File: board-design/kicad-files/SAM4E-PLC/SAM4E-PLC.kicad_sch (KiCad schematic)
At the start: 28 parts, among them J1 Conn_ARM_JTAG_SWD_10, U1 MCP7940N-xSN, U2 ATSAM4E16E, Y1 ECS-160-8-33B-CTN-TR, Y2 FC-135 32.7680KA-AG0

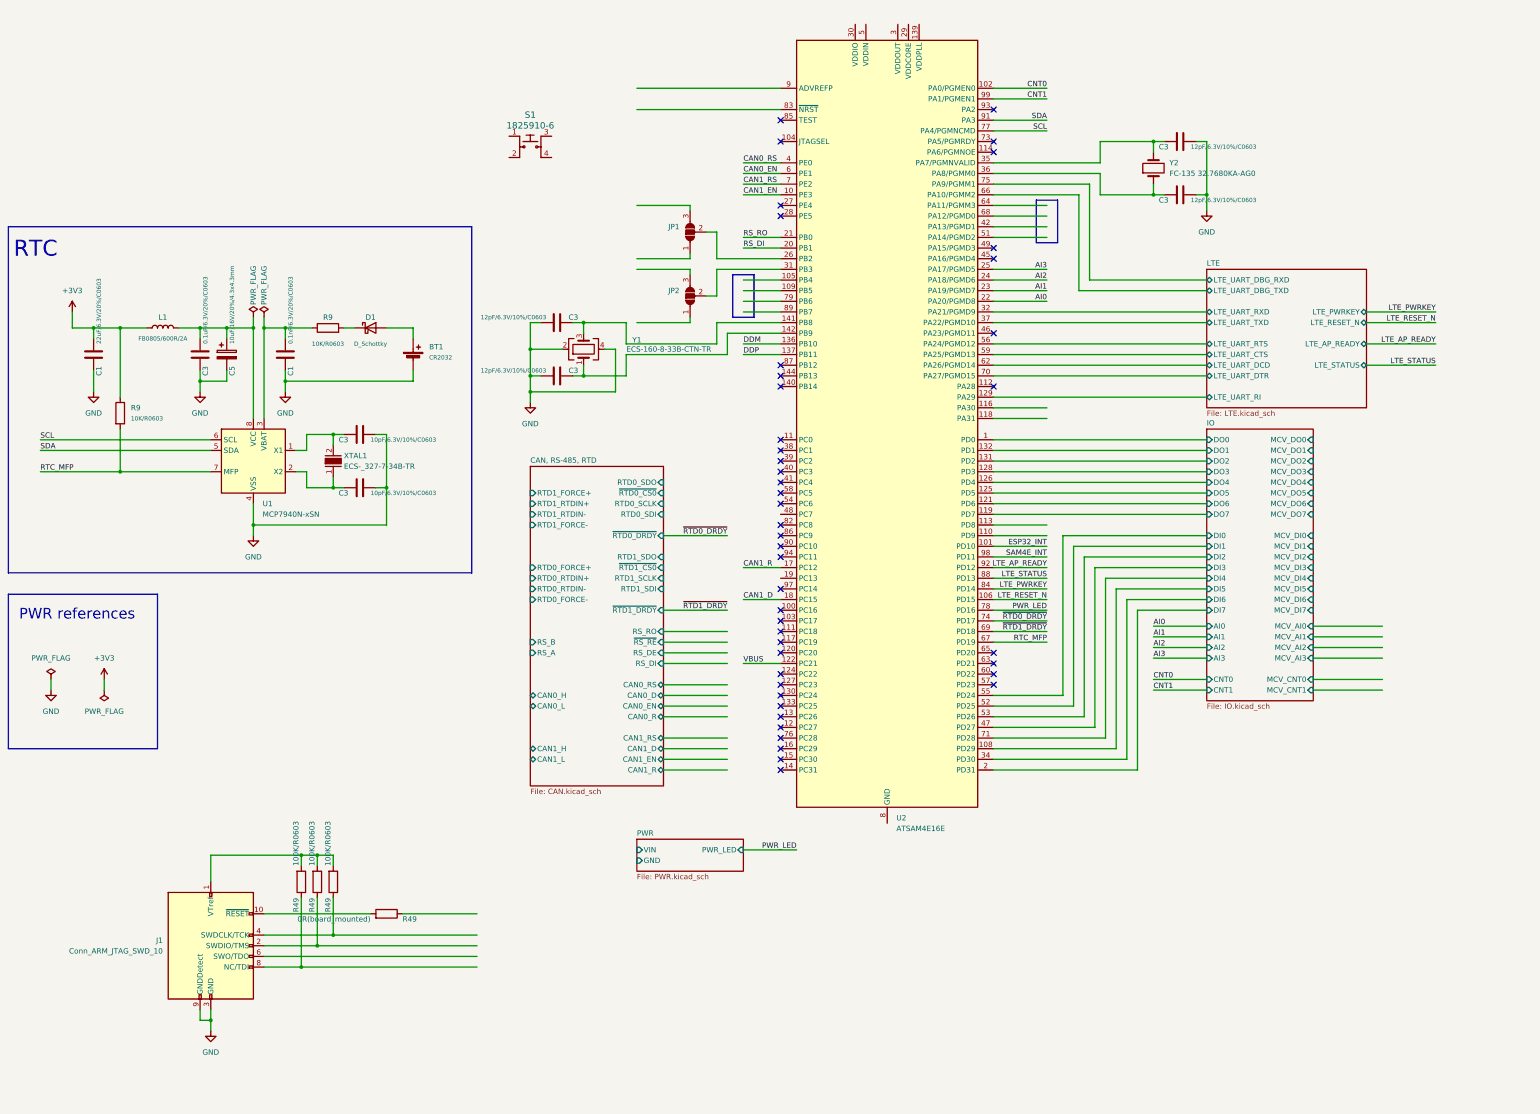
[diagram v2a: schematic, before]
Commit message: [UPDATE]
First draft of SAM4E-PLC schematic completed.

Signed-off-by: Nicolae-Andrei Vasile <vasilenicolaeandrei@gmail.com>
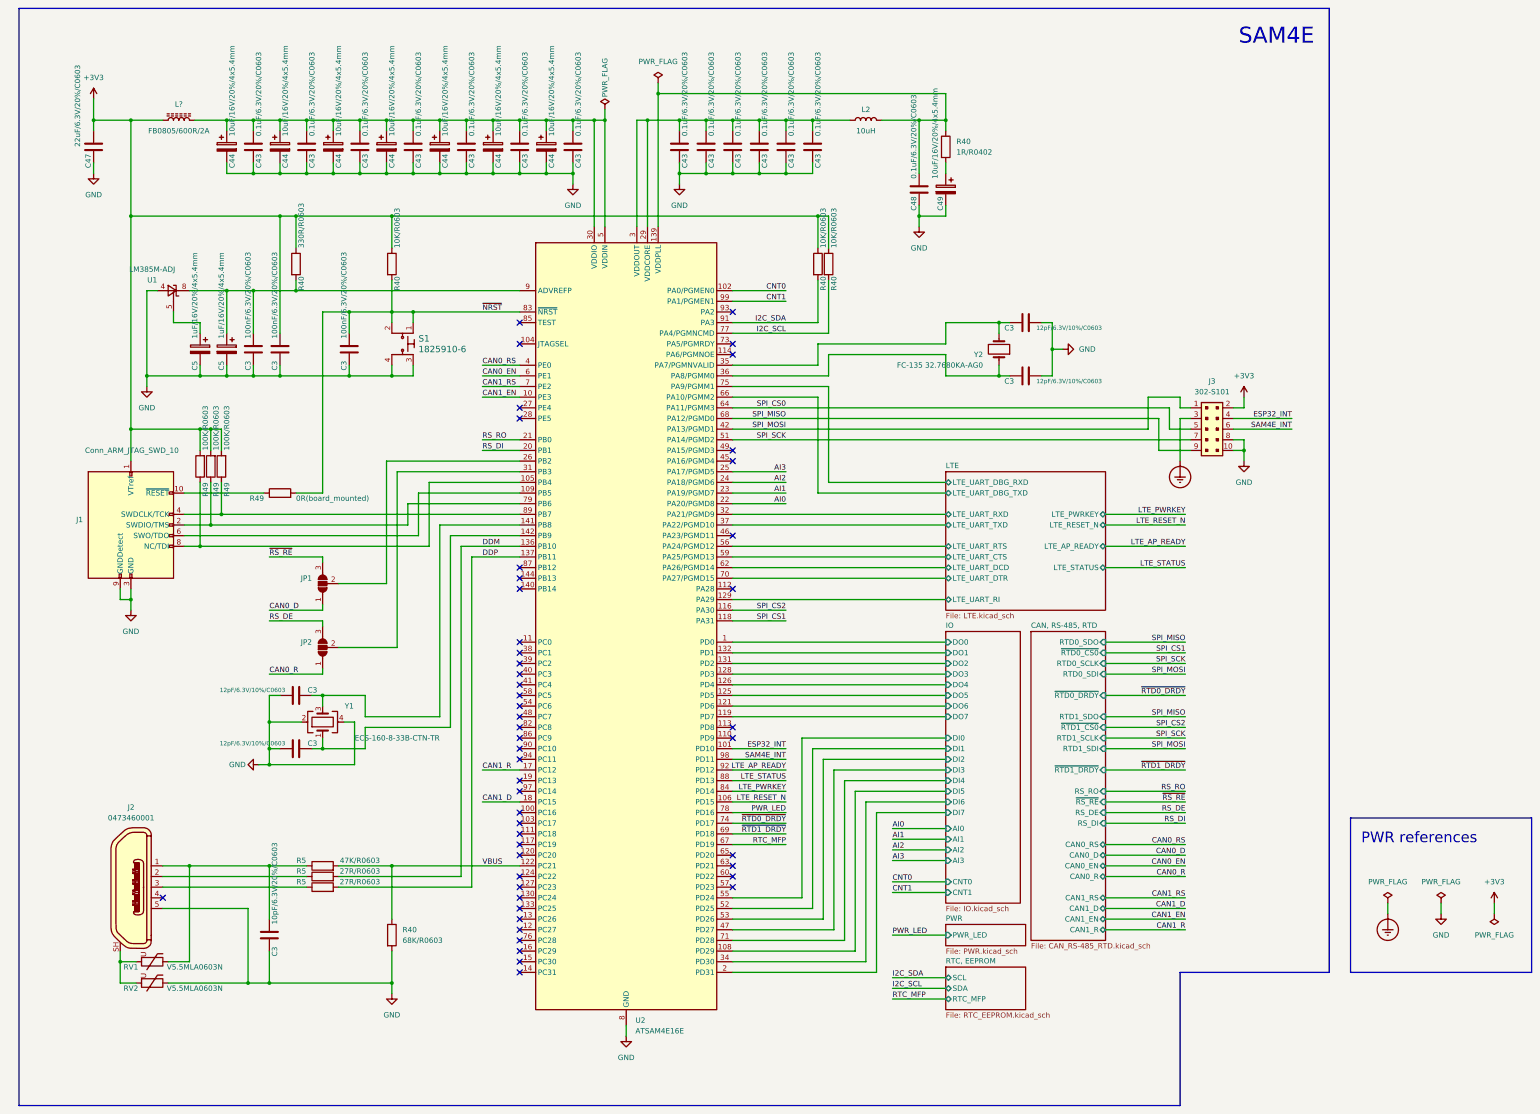
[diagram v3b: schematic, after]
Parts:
- removed BT1: CR2032, symbol Device:Battery_Cell
- removed C1: 0.1nF/6.3V/20%/C0603, symbol Device:C
- removed C1: 22uF/6.3V/20%/C0603, symbol Device:C
- removed C3 (x2): 10pF/6.3V/10%/C0603, symbol Device:C
- removed C3: 0.1uF/6.3V/20%/C0603, symbol Device:C
- removed C5: 10uF/16V/20%/4.3x4.3mm, symbol Device:C_Polarized
- removed D1: D_Schottky, symbol SparkFun-DiscreteSemi:D_Schottky
- removed L1: FB0805/600R/2A, symbol Device:L
- removed R9 (x2): 10K/R0603, symbol Device:R
- removed U1: MCP7940N-xSN, Package_SO:SOIC-8_3.9x4.9mm_P1.27mm, symbol Timer_RTC:MCP7940N-xSN
- removed XTAL1: ECS-_327-7-34B-TR, digikey-footprints:SMD-2_3.2x1.5mm, symbol dk_Crystals:ECS-_327-12_5-34B-TR
- added C3 (x3): 100nF/6.3V/20%/C0603, Capacitor_SMD:C_0603_1608Metric, symbol Device:C
- added C3: 10pF/6.3V/20%/C0603, Capacitor_SMD:C_0603_1608Metric, symbol Device:C
- added C43 (x13), C48: 0.1uF/6.3V/20%/C0603, Capacitor_SMD:C_0603_1608Metric, symbol Device:C
- added C44 (x7), C49: 10uF/16V/20%/4x5.4mm, Capacitor_SMD:CP_Elec_4x5.4, symbol Device:C_Polarized
- added C47: 22uF/6.3V/20%/C0603, Capacitor_SMD:C_0603_1608Metric, symbol Device:C
- added C5 (x2): 1uF/16V/20%/4x5.4mm, Capacitor_SMD:CP_Elec_4x5.4, symbol Device:C_Polarized
- added J2: 0473460001, digikey-footprints:USB_Micro_B_Female_0473460001, symbol dk_USB-DVI-HDMI-Connectors:0473460001
- added J3: 302-S101, Connector_IDC:IDC-Header_2x05_P2.54mm_Vertical, symbol dk_Rectangular-Connectors-Headers-Male-Pins:302-S101
- added L2: 10uH, Inductor_SMD:L_1210_3225Metric, symbol Device:L
- added L?: FB0805/600R/2A, Inductor_SMD:L_0805_2012Metric, symbol Device:L_Ferrite
- added R40 (x3): 10K/R0603, Resistor_SMD:R_0603_1608Metric, symbol Device:R
- added R40: 330R/R0603, Resistor_SMD:R_0603_1608Metric, symbol Device:R
- added R40: 1R/R0402, Resistor_SMD:R_0402_1005Metric, symbol Device:R
- added R40: 68K/R0603, Resistor_SMD:R_0603_1608Metric, symbol Device:R
- added R5 (x2): 27R/R0603, Resistor_SMD:R_0603_1608Metric, symbol Device:R
- added R5: 47K/R0603, Resistor_SMD:R_0603_1608Metric, symbol Device:R
- added RV1, RV2: V5.5MLA0603N, Resistor_SMD:R_0603_1608Metric, symbol Device:Varistor
- added U1: LM385M-ADJ, Package_SO:SOIC-8_3.9x4.9mm_P1.27mm, symbol Reference_Voltage:LM385M-ADJ
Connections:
- net +3V3: now also J1.1 (VTref), R49.2, R49.2, R49.2, C3.1, C47.1, J3.2, L?.1, R40.1, R40.1, R40.1, R40.1
- net DDM: now also R5.2
- net DDP: now also R5.2
- net ESP32_INT: now also J3.4
- net GND: now also S1.3, S1.4, U2.115 (GND), U2.135 (GND), U2.138 (GND), U2.44 (GND), U2.61 (GND), U2.8 (GND), U2.95 (GND), C3.2, C3.2, C3.2, C3.2, C43.2, C43.2, C43.2, C43.2, C43.2, C43.2, C43.2, C43.2, C43.2, C43.2, C43.2, C43.2, C43.2, C44.2, C44.2, C44.2, C44.2, C44.2, C44.2, C44.2, C47.2, C48.2, C49.2, C5.2, C5.2, J2.5, J3.10, J3.8, R40.2, RV2.1, U1.4 (A)
- net SAM4E_INT: now also J3.6
- net VBUS: now also R40.1, R5.2
- net at R49.1: now also J1.10 (~{RESET})
- net ~{NRST}: now reaches R49.2
- net ~{NRST}: now also S1.1, S1.2, U2.83 (~{NRST}), C3.1, R40.2; no longer J1.10 (~{RESET})
- net at U2.105 (PB4): now also J1.8 (NC/TDI), R49.1
- net at U2.107 (VDDCORE), U2.123 (VDDCORE), U2.29 (VDDCORE)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: now also U2.3 (VDDOUT), C43.1, C43.1, C43.1, C43.1, C43.1, C43.1, L2.1
- net at U2.109 (PB5): now also J1.6 (SWO/TDO)
- net SPI_CS2: now reaches U2.116 (PA30)
- net SPI_CS1: now reaches U2.118 (PA31)
- net at U2.134 (VDDIO), U2.143 (VDDIO), U2.30 (VDDIO)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: now also U2.5 (VDDIN), C43.1, C43.1, C43.1, C43.1, C43.1, C43.1, C43.1, C44.1, C44.1, C44.1, C44.1, C44.1, C44.1, C44.1, L?.2
- net at U2.139 (VDDPLL): now also C48.1, L2.2, R40.1
- net SPI_MOSI: now reaches U2.42 (PA13/PGMD1)
- net SPI_MOSI: now also J3.1
- net SPI_SCK: now reaches U2.51 (PA14/PGMD2)
- net SPI_SCK: now also J3.7
- net SPI_CS0: now reaches U2.64 (PA11/PGMM3)
- net SPI_CS0: now also J3.5
- net SPI_MISO: now reaches U2.68 (PA12/PGMD0)
- net SPI_MISO: now also J3.9
- net at U2.79 (PB6): now also J1.2 (SWDIO/TMS), R49.1
- net at U2.89 (PB7): now also J1.4 (SWDCLK/TCK), R49.1
- net at U2.9 (ADVREFP): now also C3.1, C5.1, R40.2, U1.8 (K)
- net CAN0_R: now reaches JP2.1 (A)
- net RS_DE: now reaches JP2.3 (B)
- net CAN0_D: now reaches JP1.1 (A)
- net ~{RS_RE}: now reaches JP1.3 (B)
- net SCL renamed I2C_SCL
- net I2C_SCL: now also R40.2
- net SDA renamed I2C_SDA
- net I2C_SDA: now also R40.2
- new net: J2.2, R5.1
- new net: C3.1, J2.1, R5.1, RV1.1
- new net: C49.1, R40.2
- new net: J2.SH, RV1.2, RV2.2
- new net: C5.1, U1.5 (FB)
- new net: J2.3, R5.1
- new net Earth_Protective: J3.3
- no-connect marks 45 -> 50
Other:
- added sheet RTC, EEPROM (RTC_EEPROM.kicad_sch)
- sheet CAN, RS-485, RTD: file CAN.kicad_sch -> CAN_RS-485_RTD.kicad_sch
- sheet CAN, RS-485, RTD ports: added none; removed CAN0_H, CAN0_L, CAN1_H, CAN1_L, RS_A, RS_B, RTD0_FORCE+, RTD0_FORCE-, RTD0_RTDIN+, RTD0_RTDIN-, RTD1_FORCE+, RTD1_FORCE-, RTD1_RTDIN+, RTD1_RTDIN-
- sheet IO ports: added none; removed MCV_AI0, MCV_AI1, MCV_AI2, MCV_AI3, MCV_CNT0, MCV_CNT1, MCV_DI0, MCV_DI1, MCV_DI2, MCV_DI3, MCV_DI4, MCV_DI5, MCV_DI6, MCV_DI7, MCV_DO0, MCV_DO1, MCV_DO2, MCV_DO3, MCV_DO4, MCV_DO5, MCV_DO6, MCV_DO7
- sheet PWR ports: added none; removed GND, VIN
- note added: "SAM4E"
- note removed: "RTC"
- moved on the sheet: C3, J1, JP1, JP2, R49, U2, Y1, Y2

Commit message: [IN PROGRESS]
SAM4E-PLC PCB design in progress.

Signed-off-by: Nicolae-Andrei Vasile <vasilenicolaeandrei@gmail.com>
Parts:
- C3: footprint (none) -> Capacitor_SMD:C_0603_1608Metric
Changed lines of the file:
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@@
       (effects (font (size 1.016 1.016)) (justify left))
     )
-    (property "Footprint" "" (at 254 93.6752 0)
+    (property "Footprint" "Capacitor_SMD:C_0603_1608Metric" (at 254 93.6752 0)
       (effects (font (size 1.27 1.27)) hide)
     )
@@
       (effects (font (size 1.016 1.016)) (justify left))
     )
-    (property "Footprint" "" (at 87.63 180.6448 0)
+    (property "Footprint" "Capacitor_SMD:C_0603_1608Metric" (at 87.63 180.6448 0)
       (effects (font (size 1.27 1.27)) hide)
     )
@@
       (effects (font (size 1.016 1.016)) (justify left))
     )
-    (property "Footprint" "" (at 87.63 193.3448 0)
+    (property "Footprint" "Capacitor_SMD:C_0603_1608Metric" (at 87.63 193.3448 0)
       (effects (font (size 1.27 1.27)) hide)
     )
@@
       (effects (font (size 1.016 1.016)) (justify left))
     )
-    (property "Footprint" "" (at 254 106.3752 0)
-      (effects (font (size 1.27 1.27)) hide)
-    )
+    (property "Footprint" "Capacitor_SMD:C_0603_1608Metric" (at 254 106.3752 0)
+      (effects (font (size 1.27 1.27)) hide)
+    )

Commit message: [UPDATE]
Work in progress.

Signed-off-by: Nicolae-Andrei Vasile <vasilenicolaeandrei@gmail.com>
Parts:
- added D1: RB068LAM-30TFTR, Diode_SMD:D_SOD-128, symbol Device:D_Schottky
- added H1, H2, H3, H4: MountingHole, MountingHole:MountingHole_2.5mm, symbol Mechanical:MountingHole
- JP1, JP2: footprint (none) -> Jumper:SolderJumper-3_P1.3mm_Open_Pad1.0x1.5mm
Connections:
- net +3V3: now also D1.2 (A); no longer J3.2
- new net: D1.1 (K), J3.2
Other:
- note added: "Mounting Holes"
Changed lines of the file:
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@@
+    (stroke (width 0) (type default))
+  )
+  (wire (pts (xy 309.88 100.33) (xy 309.88 102.87))
     (stroke (width 0) (type default))
   )
@@
     (fill (type none))
   )
+  (rectangle (start 336.55 17.78) (end 402.59 50.8)
+    (stroke (width 0) (type default) (color 140 140 0 1))
+    (fill (type none))
+  )
+  (text "Mounting Holes" (at 339.09 22.86 0)
+    (effects (font (size 2.54 2.54) (color 140 140 0 1)) (justify left bottom))
+  )
   (text "PWR references" (at 337.82 217.17 0)
     (effects (font (size 2.54 2.54) (color 140 140 0 1)) (justify left bottom))
@@
         (path "/93076d8a-73da-4f5d-b7f2-28678f1db77d"
           (reference "L1") (unit 1)
+        )
+      )
+    )
+  )
+  (symbol (lib_id "Mechanical:MountingHole") (at 350.52 43.18 0) (unit 1)
+    (in_bom yes) (on_board yes) (dnp no) (fields_autoplaced)
+    (property "Reference" "H2" (at 353.06 41.91 0)
+      (effects (font (size 1.27 1.27)) (justify left))
+    )
+    (property "Value" "MountingHole" (at 353.06 44.45 0)
+      (effects (font (size 1.27 1.27)) (justify left))
+    )
+    (property "Footprint" "MountingHole:MountingHole_2.5mm" (at 350.52 43.18 0)
+      (effects (font (size 1.27 1.27)) hide)
+    )
+    (property "Datasheet" "~" (at 350.52 43.18 0)
+      (effects (font (size 1.27 1.27)) hide)
+    )
+    (instances
+      (project "SAM4E-PLC"
+        (path "/93076d8a-73da-4f5d-b7f2-28678f1db77d"
+          (reference "H2") (unit 1)
         )
       )
@@
         (path "/93076d8a-73da-4f5d-b7f2-28678f1db77d"
           (reference "C5") (unit 1)
+        )
+      )
+    )
+  )
+  (symbol (lib_id "Device:D_Schottky") (at 309.88 106.68 90) (unit 1)
+    (in_bom yes) (on_board yes) (dnp no) (fields_autoplaced)
+    (property "Reference" "D1" (at 312.42 105.7275 90)
+      (effects (font (size 1.27 1.27)) (justify right))
+    )
+    (property "Value" "RB068LAM-30TFTR" (at 312.42 108.2675 90)
+      (effects (font (size 1.27 1.27)) (justify right))
+    )
+    (property "Footprint" "Diode_SMD:D_SOD-128" (at 309.88 106.68 0)
+      (effects (font (size 1.27 1.27)) hide)
+    )
+    (property "Datasheet" "https://fscdn.rohm.com/en/products/databook/datasheet/discrete/diode/schottky_barrier/rb068lam-30tftr-e.pdf" (at 309.88 106.68 0)
+      (effects (font (size 1.27 1.27)) hide)
+    )
+    (pin "1")
+    (pin "2")
+    (instances
+      (project "SAM4E-PLC"
+        (path "/93076d8a-73da-4f5d-b7f2-28678f1db77d"
+          (reference "D1") (unit 1)
         )
       )
@@
     )
   )
+  (symbol (lib_id "Mechanical:MountingHole") (at 350.52 31.75 0) (unit 1)
+    (in_bom yes) (on_board yes) (dnp no) (fields_autoplaced)
+    (property "Reference" "H1" (at 353.06 30.48 0)
+      (effects (font (size 1.27 1.27)) (justify left))
+    )
+    (property "Value" "MountingHole" (at 353.06 33.02 0)
+      (effects (font (size 1.27 1.27)) (justify left))
+    )
+    (property "Footprint" "MountingHole:MountingHole_2.5mm" (at 350.52 31.75 0)
+      (effects (font (size 1.27 1.27)) hide)
+    )
+    (property "Datasheet" "~" (at 350.52 31.75 0)
+      (effects (font (size 1.27 1.27)) hide)
+    )
+    (instances
+      (project "SAM4E-PLC"
+        (path "/93076d8a-73da-4f5d-b7f2-28678f1db77d"
+          (reference "H1") (unit 1)
+        )
+      )
+    )
+  )
   (symbol (lib_id "Device:R") (at 63.5 127 180) (unit 1)
     (in_bom yes) (on_board yes) (dnp no)
@@
     )
   )
+  (symbol (lib_id "Mechanical:MountingHole") (at 375.92 43.18 0) (unit 1)
+    (in_bom yes) (on_board yes) (dnp no) (fields_autoplaced)
+    (property "Reference" "H4" (at 378.46 41.91 0)
+      (effects (font (size 1.27 1.27)) (justify left))
+    )
+    (property "Value" "MountingHole" (at 378.46 44.45 0)
+      (effects (font (size 1.27 1.27)) (justify left))
+    )
+    (property "Footprint" "MountingHole:MountingHole_2.5mm" (at 375.92 43.18 0)
+      (effects (font (size 1.27 1.27)) hide)
+    )
+    (property "Datasheet" "~" (at 375.92 43.18 0)
+      (effects (font (size 1.27 1.27)) hide)
+    )
+    (instances
+      (project "SAM4E-PLC"
+        (path "/93076d8a-73da-4f5d-b7f2-28678f1db77d"
+          (reference "H4") (unit 1)
+        )
+      )
+    )
+  )
   (symbol (lib_id "power:GND") (at 106.68 252.73 0) (unit 1)
     (in_bom yes) (on_board yes) (dnp no) (fields_autoplaced)
@@
     )
   )
-  (symbol (lib_id "power:+3V3") (at 309.88 110.49 0) (unit 1)
+  (symbol (lib_id "power:+3V3") (at 309.88 100.33 0) (unit 1)
     (in_bom yes) (on_board yes) (dnp no) (fields_autoplaced)
-    (property "Reference" "#PWR01" (at 309.88 114.3 0)
-      (effects (font (size 1.27 1.27)) hide)
-    )
-    (property "Value" "+3V3" (at 309.88 105.41 0)
-      (effects (font (size 1.27 1.27)))
-    )
-    (property "Footprint" "" (at 309.88 110.49 0)
-      (effects (font (size 1.27 1.27)) hide)
-    )
-    (property "Datasheet" "" (at 309.88 110.49 0)
+    (property "Reference" "#PWR01" (at 309.88 104.14 0)
+      (effects (font (size 1.27 1.27)) hide)
+    )
+    (property "Value" "+3V3" (at 309.88 95.25 0)
+      (effects (font (size 1.27 1.27)))
+    )
+    (property "Footprint" "" (at 309.88 100.33 0)
+      (effects (font (size 1.27 1.27)) hide)
+    )
+    (property "Datasheet" "" (at 309.88 100.33 0)
       (effects (font (size 1.27 1.27)) hide)
     )
@@
       (effects (font (size 1.27 1.27)) (justify left) hide)
     )
-    (property "Footprint" "" (at 90.17 170.18 0)
+    (property "Footprint" "Jumper:SolderJumper-3_P1.3mm_Open_Pad1.0x1.5mm" (at 90.17 170.18 0)
       (effects (font (size 1.27 1.27)) hide)
     )
@@
     )
   )
+  (symbol (lib_id "Mechanical:MountingHole") (at 375.92 31.75 0) (unit 1)
+    (in_bom yes) (on_board yes) (dnp no) (fields_autoplaced)
+    (property "Reference" "H3" (at 378.46 30.48 0)
+      (effects (font (size 1.27 1.27)) (justify left))
+    )
+    (property "Value" "MountingHole" (at 378.46 33.02 0)
+      (effects (font (size 1.27 1.27)) (justify left))
+    )
+    (property "Footprint" "MountingHole:MountingHole_2.5mm" (at 375.92 31.75 0)
+      (effects (font (size 1.27 1.27)) hide)
+    )
+    (property "Datasheet" "~" (at 375.92 31.75 0)
+      (effects (font (size 1.27 1.27)) hide)
+    )
+    (instances
+      (project "SAM4E-PLC"
+        (path "/93076d8a-73da-4f5d-b7f2-28678f1db77d"
+          (reference "H3") (unit 1)
+        )
+      )
+    )
+  )
   (symbol (lib_id "Device:C") (at 257.81 105.41 270) (unit 1)
     (in_bom yes) (on_board yes) (dnp no)
@@
       (effects (font (size 1.27 1.27)) (justify left) hide)
     )
-    (property "Footprint" "" (at 90.17 154.94 0)
-      (effects (font (size 1.27 1.27)) hide)
-    )
+    (property "Footprint" "Jumper:SolderJumper-3_P1.3mm_Open_Pad1.0x1.5mm" (at 90.17 154.94 0)
+      (effects (font (size 1.27 1.27)) hide)
+    )

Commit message: [UPDATE]
Work in progress.

Signed-off-by: Nicolae-Andrei Vasile <vasilenicolaeandrei@gmail.com>
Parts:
- added C43: 0.1uF/6.3V/20%/C0603, Capacitor_SMD:C_0603_1608Metric, symbol Device:C
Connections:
- net GND: now also C43.2
- net at C43.1, C43.1, C43.1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: now also C43.1
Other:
- moved on the sheet: C48, C49, L2, R40
